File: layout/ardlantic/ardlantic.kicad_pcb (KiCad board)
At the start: 2 copper layers, 45.7 x 43.2 mm, 13 parts, among them J1 (DC) PowerSupply, J2 OnOffSensor, J3 (IR) IR Input, J4 Shield NRF24 Input, J5 Shield NRF24 PowerSupply, J6 Shield NRF24 Output, J7 (TEMP) Temp Input, U1 Arduino Pro Micro

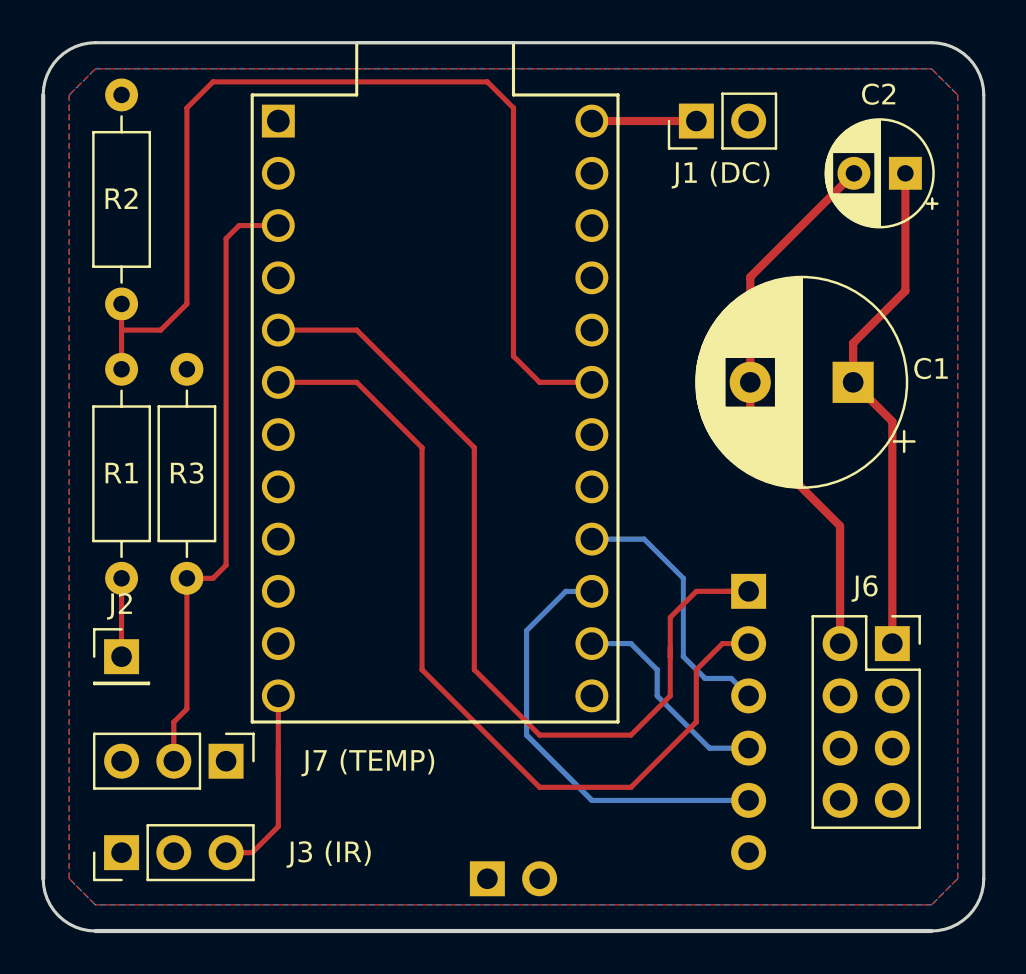
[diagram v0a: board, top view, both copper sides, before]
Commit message: New layout revision with fix + fix mysensor pin + add temperature sensor
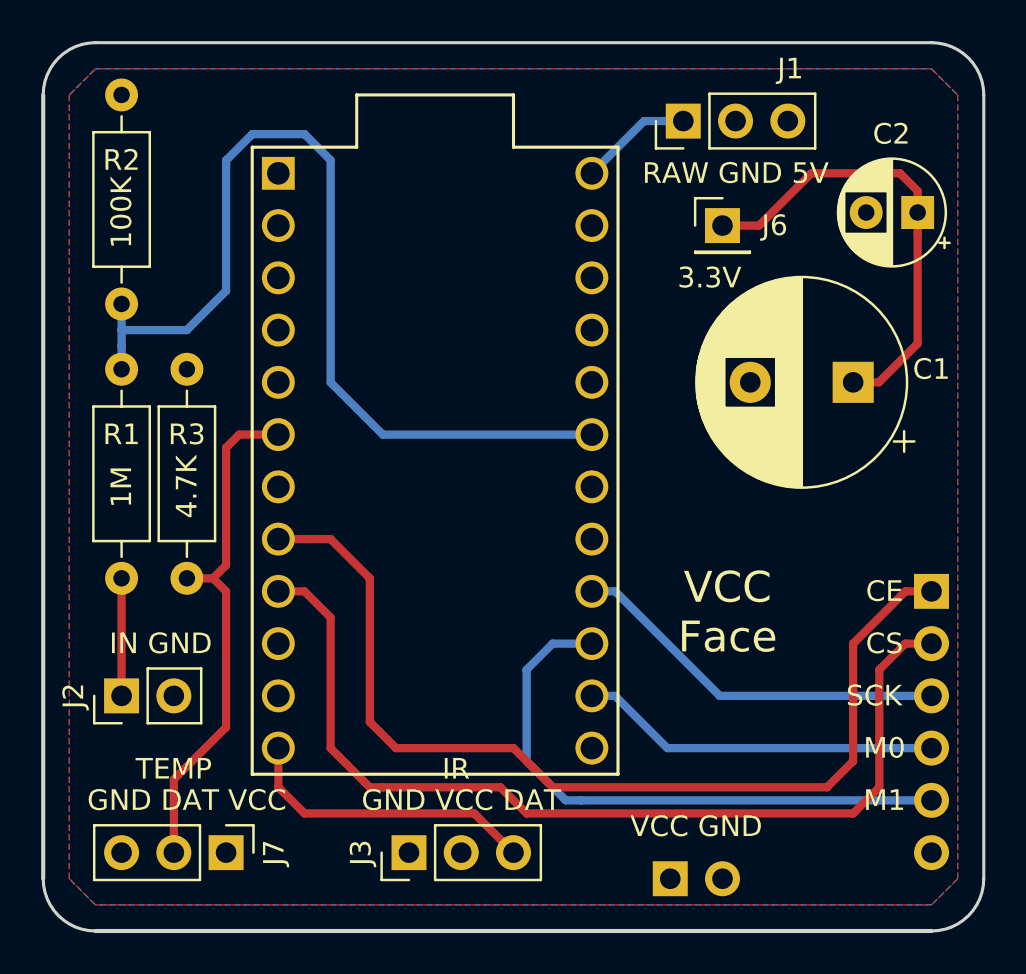
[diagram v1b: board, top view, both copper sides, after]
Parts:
- removed J1 (DC): PowerSupply, Connector_PinHeader_2.54mm:PinHeader_1x02_P2.54mm_Vertical
- removed J3 (IR): IR Input, Connector_PinHeader_2.54mm:PinHeader_1x03_P2.54mm_Vertical
- removed J7 (TEMP): Temp Input, Connector_PinHeader_2.54mm:PinHeader_1x03_P2.54mm_Vertical
- added J1: PowerSupply, Connector_PinHeader_2.54mm:PinHeader_1x03_P2.54mm_Vertical, F.Cu at (128.9, 53.3)
- added J3: IR Input, Connector_PinHeader_2.54mm:PinHeader_1x03_P2.54mm_Vertical, F.Cu at (115.6, 88.9)
- added J7: Temp Input, Connector_PinHeader_2.54mm:PinHeader_1x03_P2.54mm_Vertical, F.Cu at (106.7, 88.9)
- J2: value OnOffSensor -> OnOffSensor Input; footprint Connector_PinHeader_2.54mm:PinHeader_1x01_P2.54mm_Vertical -> Connector_PinHeader_2.54mm:PinHeader_1x02_P2.54mm_Vertical
- J4: value Shield NRF24 Input -> Shield NRF24 Output; footprint Connector_PinSocket_2.54mm:PinSocket_1x06_P2.54mm_Vertical -> Connector_PinHeader_2.54mm:PinHeader_1x06_P2.54mm_Vertical
- J6: value Shield NRF24 Output -> Shield NRF24 VCC; footprint Connector_PinSocket_2.54mm:PinSocket_2x04_P2.54mm_Vertical -> Connector_PinHeader_2.54mm:PinHeader_1x01_P2.54mm_Vertical
- moved J6 21.9 mm to (130.8, 58.4)
- moved J5 8.89 mm to (128.3, 90.2)
- moved J4 8.89 mm to (141.0, 76.2)
- moved U1 2.54 mm to (116.8, 69.8)
- moved C2 2.00 mm to (140.3, 57.8)
- moved J2 1.91 mm to (101.6, 81.3), turned to 90 degrees
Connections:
- net Net-(C1-Pad1) renamed /3.3V
- net Net-(J2-Pad1) renamed /IN
- C1 pad 2: /GND_NRF -> GND
- C2 pad 2: /GND_NRF -> GND
- J4 pad 6: Net-(J4-Pad6) -> (no net)
- U1 pad 1: Net-(U1-Pad1) -> (no net)
- U1 pad 10: Net-(U1-Pad10) -> (no net)
- U1 pad 11: Net-(U1-Pad11) -> (no net)
- U1 pad 13: Net-(U1-Pad13) -> (no net)
- U1 pad 17: Net-(U1-Pad17) -> (no net)
- U1 pad 18: Net-(U1-Pad18) -> (no net)
- U1 pad 2: Net-(U1-Pad2) -> (no net)
- U1 pad 20: Net-(U1-Pad20) -> (no net)
- U1 pad 22: Net-(U1-Pad22) -> (no net)
- U1 pad 23: Net-(U1-Pad23) -> GND
- U1 pad 24: /VDC -> /RAW
- U1 pad 3: /TDATA -> GND
- U1 pad 4: Net-(U1-Pad4) -> GND
- U1 pad 5: /CE -> (no net)
- U1 pad 6: /CS -> /TDATA
- U1 pad 7: Net-(U1-Pad7) -> (no net)
- U1 pad 8: Net-(U1-Pad8) -> /CE
- U1 pad 9: Net-(U1-Pad9) -> /CS
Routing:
- net /GND_NRF: track 26.8 -> 0.00 mm
- net /M1: track 21.2 -> 28.6 mm
- net /M0: track 10.5 -> 17.8 mm
- net /RAW: track 0.00 -> 5.50 mm
- net /SCK: track 13.0 -> 18.5 mm
- net /VDC: track 5.08 -> 0.00 mm
- net /CS: track 41.7 -> 46.7 mm
- net /TDATA: track 30.0 -> 25.3 mm
- net /CE: track 44.0 -> 48.1 mm
- net /DAT: track 10.7 -> 14.7 mm
- net Net-(R1-Pad2): track 49.7 -> 46.1 mm
- net /3.3V: track 24.7 -> 22.2 mm, vias 0 -> 1
- net /IN: track 3.81 -> 5.72 mm
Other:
- board text added: "100K"
- board text added: "14"
- board text added: "15"
- board text added: "16"
- board text added: "1M"
- board text added: "3.3V"
- board text added: "4.7K"
- board text added: "5"
- board text added: "6"
- board text added: "9"
- board text added: "A2"
- board text added: "Ardlantic Revision 2"
- board text added: "CE"
- board text added: "CS"
- board text added: "DAT VCC GND"
- board text added: "GND"
- board text added: "GND DAT VCC"
- board text added: "GND Face"
- board text added: "GND IN"
- board text added: "GND VCC DAT"
- board text added: "IN GND"
- board text added: "IR"
- board text added: "M0"
- board text added: "M1"
- board text added: "RAW"
- board text added: "RAW GND 5V"
- board text added: "RST"
- board text added: "SCK"
- board text added: "TEMP"
- board text added: "VCC"
- board text added: "VCC DAT GND"
- board text added: "VCC Face"
- board text added: "VCC GND"
- board text added: "VCC GND RAW"
- board text removed: "Ardlantic Revision 1"
